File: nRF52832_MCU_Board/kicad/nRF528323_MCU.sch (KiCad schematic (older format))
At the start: 34 parts, among them J6 CONN_02X05, J7 CONN_01X05, J8 MM8130-2600, X1 32MHz, X2 32.768kHz

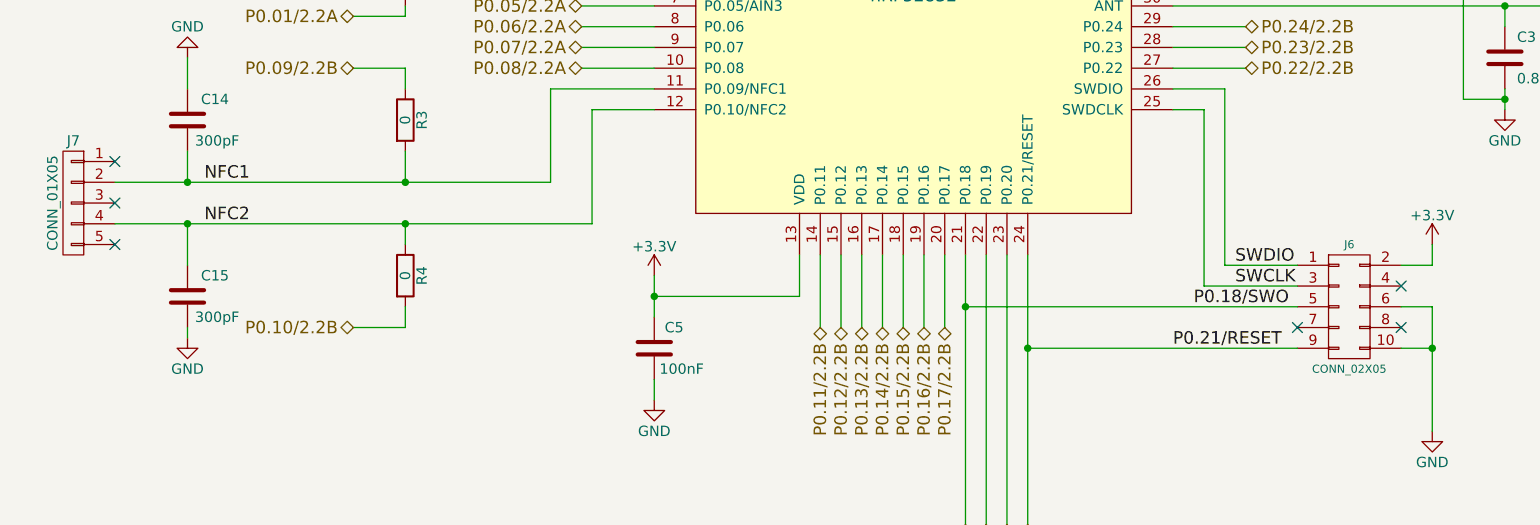
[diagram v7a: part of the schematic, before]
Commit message: Update nRF52832_MCU_Board
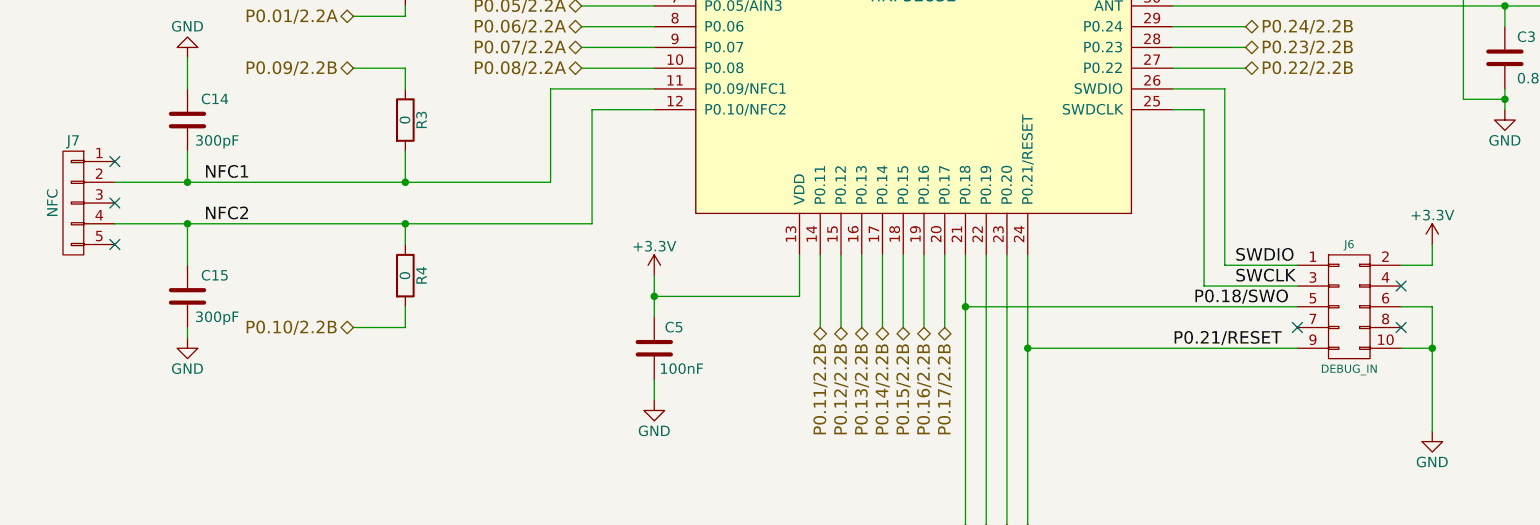
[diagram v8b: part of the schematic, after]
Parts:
- J6: value CONN_02X05 -> DEBUG_IN
- J7: value CONN_01X05 -> NFC
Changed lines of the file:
@@
 EESchema Schematic File Version 2
+LIBS:nRF52832_MCU_Board-rescue
 LIBS:Nordic_misc
 LIBS:Nordic_nRF
@@
 LIBS:Zilog
 LIBS:nRF52832_MCU_Board-cache
-EELAYER 25 0
+EELAYER 26 0
 EELAYER END
 $Descr USLetter 11000 8500
@@
 P 1350 4400
 F 0 "J7" H 1350 4700 50  0000 C CNN
-F 1 "CONN_01X05" V 1450 4400 50  0000 C CNN
+F 1 "NFC" V 1450 4400 50  0000 C CNN
 F 2 "Nordic_misc:Nordic_misc-FPC_05P-RA-SMD" H 1350 4400 50  0001 C CNN
 F 3 "" H 1350 4400 50  0001 C CNN
@@
 P 7500 4900
 F 0 "J6" H 7500 5200 39  0000 C CNN
-F 1 "CONN_02X05" H 7500 4600 39  0000 C CNN
+F 1 "DEBUG_IN" H 7500 4600 39  0000 C CNN
 F 2 "Nordic_misc:ftsh-105-01-l-dv" H 7500 3700 50  0001 C CNN
 F 3 "" H 7500 3700 50  0001 C CNN
